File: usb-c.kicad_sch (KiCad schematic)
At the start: 1 part, among them J2 USB-C_GCT_USB4105-GF-A

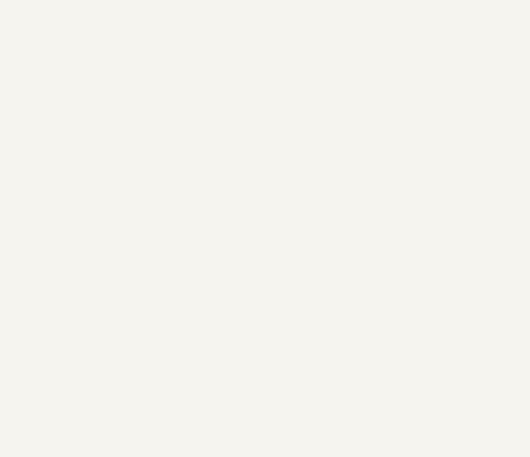
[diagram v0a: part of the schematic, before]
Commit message: [#94684] Add ports to subsheets
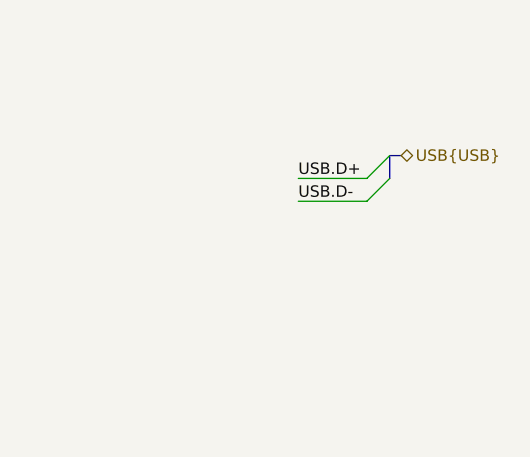
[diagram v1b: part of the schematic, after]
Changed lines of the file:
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@@
 	(generator "eeschema")
 	(generator_version "9.0")
-	(paper "A4")
+	(paper "A3")
 	(title_block
 		(title "renode-reference-platform")
@@
 		(company "Antmicro")
 	)
+	(bus_entry
+		(at 215.9 80.01)
+		(size -2.54 2.54)
+		(stroke
+			(width 0)
+			(type default)
+		)
+	)
+	(bus_entry
+		(at 215.9 77.47)
+		(size -2.54 2.54)
+		(stroke
+			(width 0)
+			(type default)
+		)
+	)
+	(wire
+		(pts
+			(xy 205.74 80.01) (xy 213.36 80.01)
+		)
+		(stroke
+			(width 0)
+			(type default)
+		)
+	)
+	(bus
+		(pts
+			(xy 217.17 77.47) (xy 215.9 77.47)
+		)
+		(stroke
+			(width 0)
+			(type default)
+		)
+	)
+	(wire
+		(pts
+			(xy 205.74 82.55) (xy 213.36 82.55)
+		)
+		(stroke
+			(width 0)
+			(type default)
+		)
+	)
+	(bus
+		(pts
+			(xy 215.9 77.47) (xy 215.9 80.01)
+		)
+		(stroke
+			(width 0)
+			(type default)
+		)
+	)
+	(label "USB.D+"
+		(at 205.74 80.01 0)
+		(effects
+			(font
+				(size 1.27 1.27)
+			)
+			(justify left bottom)
+		)
+	)
+	(label "USB.D-"
+		(at 205.74 82.55 0)
+		(effects
+			(font
+				(size 1.27 1.27)
+			)
+			(justify left bottom)
+		)
+	)
+	(hierarchical_label "USB{USB}"
+		(shape bidirectional)
+		(at 217.17 77.47 0)
+		(effects
+			(font
+				(size 1.27 1.27)
+			)
+			(justify left)
+		)
+	)
 	(symbol

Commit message: [#94911] Add USB DRP
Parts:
- added C42, C44, C45: C_100n_0402, antmicro-footprints:C_0402_1005Metric, symbol antmicroCapacitors0402:C_100n_0402
- added C43: C_4u7_6.3V_0402, antmicro-footprints:C_0402_1005Metric, symbol antmicroCapacitors0402:C_4u7_6.3V_0402
- added D10: PESD5Z5_0F, antmicro-footprints:SOD-523, symbol antmicroTVSDiodes:PESD5Z5_0F
- added D11: TPD2E009_SOT-9X3, antmicro-footprints:SOT-723, symbol antmicroTVSDiodes:TPD2E009_SOT-9X3
- added D8: PRTR5V0U2X, antmicro-footprints:SOT-143-4, symbol antmicroTVSDiodes:PRTR5V0U2X
- added D9: LED_G_0603_LTST-C190GKT, antmicro-footprints:LED_0603_1608Metric_G, symbol antmicroLEDIndicationDiscrete:LED_G_0603_LTST-C190GKT
- added R100, R101, R79, R92, R93, R94, R99: R_0R_0402, antmicro-footprints:R_0402_1005Metric, symbol antmicroResistors0402:R_0R_0402
- added R102, R103: R_100R_0402, antmicro-footprints:R_0402_1005Metric, symbol antmicroResistors0402:R_100R_0402
- added R81: R_330R_0402, antmicro-footprints:R_0402_1005Metric, symbol antmicroResistors0402:R_330R_0402
- added R82: R_12k1_0402, antmicro-footprints:R_0402_1005Metric, symbol antmicroResistors0402:R_12k1_0402
- added R83, R90, R91: R_10k_0402, antmicro-footprints:R_0402_1005Metric, symbol antmicroResistors0402:R_10k_0402
- added R84, R85, R86, R87, R88, R89, R95, R96, R97, R98: R_887k_0402, antmicro-footprints:R_0402_1005Metric, symbol antmicroResistors0402:R_887k_0402
- added TP25, TP26: TP_1mm_SMD, antmicro-footprints:TP_SMD_1mm, symbol antmicroTestPoints:TP_1mm_SMD
- added U12: FUSB303B, antmicro-footprints:Texas_X2QFN-12_1.6x1.6mm_P0.4mm, symbol antmicroInterfaceControllers:FUSB303B
- added U13: AP22615B_TSOT26, antmicro-footprints:TSOT23-6, symbol antmicroPMICPowerDistributionSwitchesLoadDrivers:AP22615B_TSOT26
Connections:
- net USB.D+: now also D8.2 (IO1), R102.2
- net USB.D-: now also D8.3 (IO2), R103.2
- net GND: now reaches J2.A1 (GND), J2.A12 (GND), J2.B1 (GND), J2.B12 (GND)
- net GND: now also J2.SH, C42.1, C43.1, C44.1, C45.1, D10.2 (A), D11.3, D8.1 (GND), D9.1 (C), R82.2, R83.2, R85.1, R87.1, R89.1, R96.1, R98.1, U12.10 (GND), U13.2 (GND)
- net USB_VBUS: now reaches J2.A4 (VBUS), J2.A9 (VBUS), J2.B4 (VBUS), J2.B9 (VBUS)
- net USB_VBUS: now also C42.2, C43.2, D10.1 (C), D8.4 (VCC), R79.2, R81.2, U12.4 (VBUS_{DET}), U13.1 (OUT)
- net CC1: now reaches J2.A5 (CC_{1})
- net CC1: now also D11.1, U12.1 (CC1)
- net at J2.A6 (D_{A}+): now also J2.B6 (D_{B}+), R102.1
- net at J2.A7 (D_{A}-): now also J2.B7 (D_{B}-), R103.1
- net CC2: now reaches J2.B5 (CC_{2})
- net CC2: now also D11.2, U12.2 (CC2)
- new net: R88.1, R89.2, R92.1, R99.1, U12.6 (~{INT}/OUT3)
- new net: R82.1, U13.5 (ISET)
- new net: R100.1, R86.1, R87.2, R93.1, U12.7 (SDA/OUT1)
- new net: R101.1, R84.1, R85.2, R94.1, U12.8 (SCL/OUT2)
- new net: D9.2 (A), R81.1
- new net: R83.1, U12.11 (~{EN})
- new net +3V3: C44.2, R84.2, R86.2, R88.2, R90.1, R91.1, R95.2, R97.2, U12.12 (V_{DD})
- new net +5V: C45.2, U13.6 (IN)
- new net ADDR/ORIENT: R95.1, R96.2, TP25.1, U12.5 (ADDR/ORIENT)
- new net FLG: R90.2, U13.3 (FLG)
- new net I2C_USB.SCL: R94.2
- new net I2C_USB.SDA: R93.2
- new net I2C_USB.~{INT}: R92.2
- new net PORT/~{DEBUG}: R97.1, R98.2, TP26.1, U12.3 (PORT/~{DEBUG})
- new net USB.ID: R91.2, U12.9 (ID), U13.4 (~{EN})
- new net USB.VBUS: R79.1
- new net USB_GPIO_OUT1: R100.2
- new net USB_GPIO_OUT2: R101.2
- new net USB_GPIO_~{INT}: R99.2
- no-connect marks 0 -> 2
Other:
- note added: "R95 - I2C mode address 62h R96 - I2C mode address 42h DNP both for GPIO mode"
- note added: "R97 - Source only R98 - Sink only DNP both for Dual Role Port"
- note added: "limit set to 0.5A"
- moved on the sheet: J2

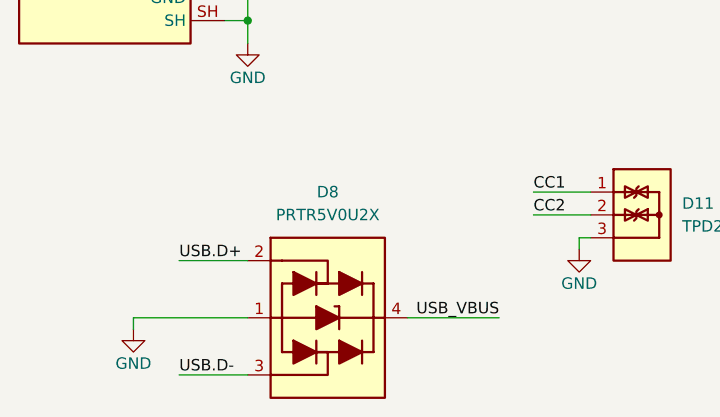
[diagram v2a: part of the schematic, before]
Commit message: [#95008] Change USB-C data lines ESD protection
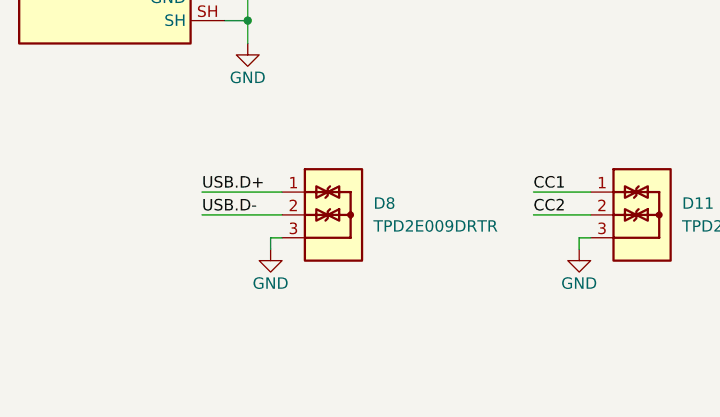
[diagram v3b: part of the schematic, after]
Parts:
- removed D8: PRTR5V0U2X, antmicro-footprints:SOT-143-4, symbol antmicroTVSDiodes:PRTR5V0U2X
- added D8: TPD2E009_SOT-9X3, antmicro-footprints:SOT-723, symbol antmicroTVSDiodes:TPD2E009_SOT-9X3
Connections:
- net GND: now also D8.3
- net USB.D+: now also D8.1
- net USB.D-: now also D8.2

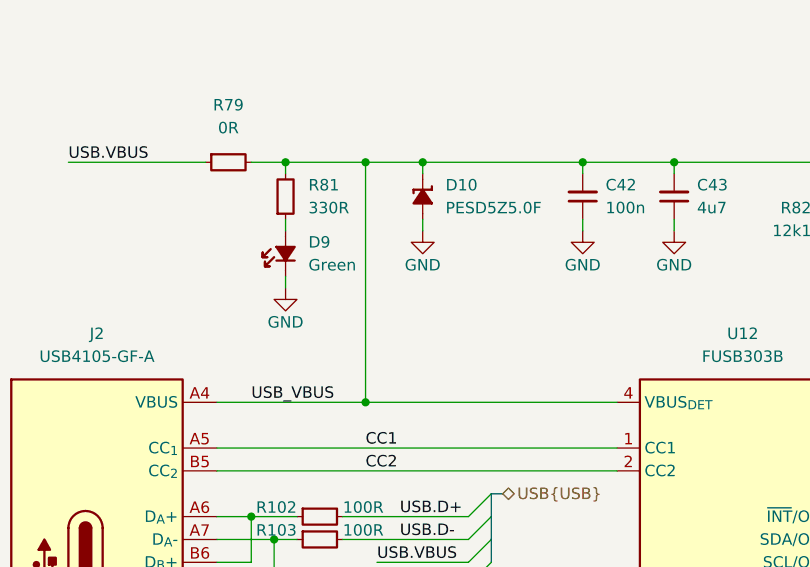
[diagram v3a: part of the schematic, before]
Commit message: [#95036] Reconnect power flags, add GPIOs to RPI connector
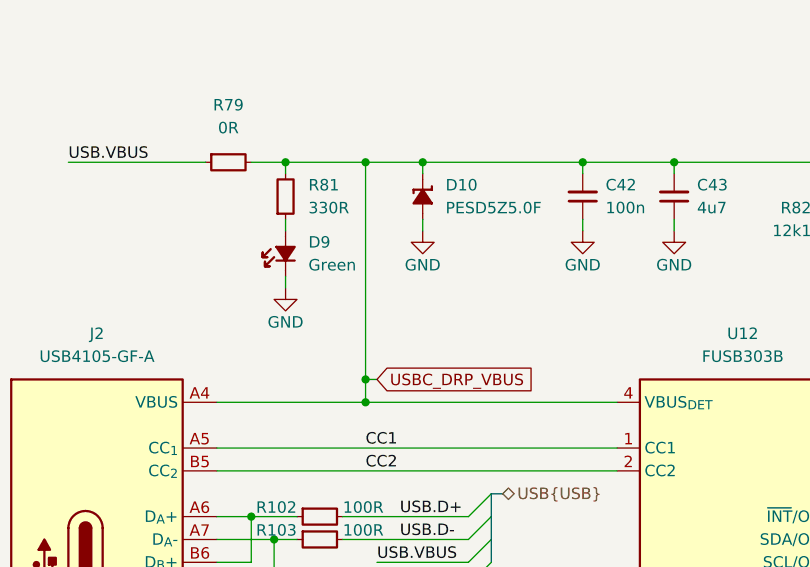
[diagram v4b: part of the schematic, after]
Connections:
- net USB_VBUS renamed USBC_DRP_VBUS
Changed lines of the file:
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@@
+	)
+	(junction
+		(at 144.78 104.14)
+		(diameter 0)
+		(color 0 0 0 0)
 	)
 	(junction
@@
 	(wire
 		(pts
+			(xy 146.05 104.14) (xy 144.78 104.14)
+		)
+		(stroke
+			(width 0)
+			(type default)
+		)
+	)
+	(wire
+		(pts
 			(xy 284.48 168.91) (xy 314.96 168.91)
 		)
@@
 	(wire
 		(pts
-			(xy 144.78 80.01) (xy 144.78 106.68)
+			(xy 144.78 80.01) (xy 144.78 104.14)
 		)
 		(stroke
@@
 		(pts
 			(xy 215.9 82.55) (xy 241.3 82.55)
+		)
+		(stroke
+			(width 0)
+			(type default)
+		)
+	)
+	(wire
+		(pts
+			(xy 144.78 104.14) (xy 144.78 106.68)
 		)
 		(stroke
@@
 		)
 	)
-	(label "USB_VBUS"
-		(at 132.08 106.68 0)
-		(effects
-			(font
-				(size 1.27 1.27)
-			)
-			(justify left bottom)
-		)
-	)
 	(label "USB.ID"
 		(at 222.25 85.09 0)
@@
 		)
 	)
+	(global_label "USBC_DRP_VBUS"
+		(shape input)
+		(at 146.05 104.14 0)
+		(fields_autoplaced yes)
+		(effects
+			(font
+				(size 1.27 1.27)
+				(thickness 0.1588)
+			)
+			(justify left)
+		)
+		(property "Intersheetrefs" "${INTERSHEET_REFS}"
+			(at 164.759 104.14 0)
+			(effects
+				(font
+					(size 1.27 1.27)
+				)
+				(justify left)
+			)
+		)
+	)

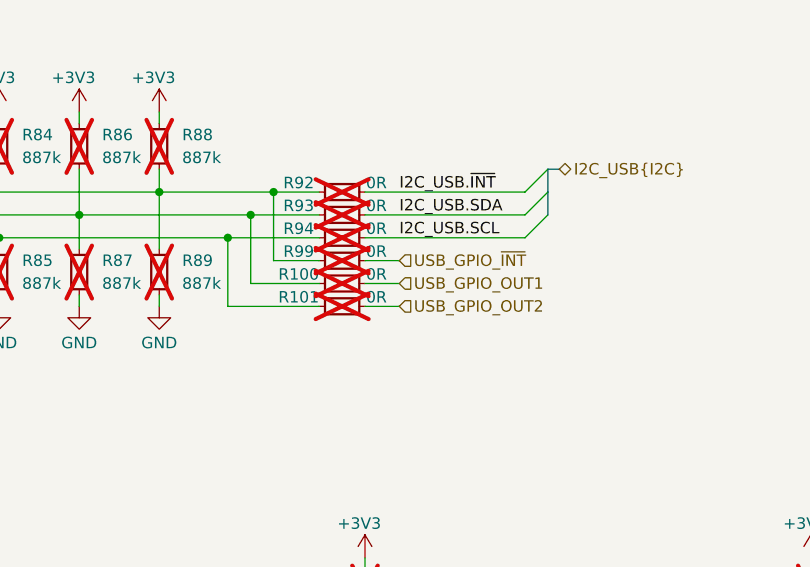
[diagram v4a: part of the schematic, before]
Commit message: [#95036] Manage I2C, UART, SPI interfaces for RPI and PMOD connectors
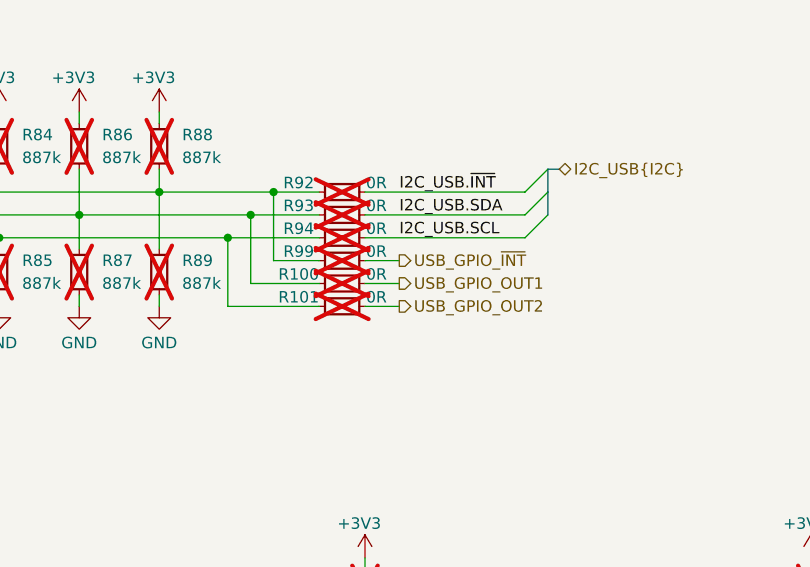
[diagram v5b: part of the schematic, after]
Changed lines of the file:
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@@
 	)
 	(hierarchical_label "USB_GPIO_~{INT}"
-		(shape input)
+		(shape output)
 		(at 269.24 127 0)
 		(effects
@@
 	)
 	(hierarchical_label "USB_GPIO_OUT1"
-		(shape input)
+		(shape output)
 		(at 269.24 129.54 0)
 		(effects
@@
 	)
 	(hierarchical_label "USB_GPIO_OUT2"
-		(shape input)
+		(shape output)
 		(at 269.24 132.08 0)
 		(effects

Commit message: [#95036] Add CAN bus subsheet
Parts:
- removed C43: C_4u7_6.3V_0402, antmicro-footprints:C_0402_1005Metric, symbol antmicroCapacitors0402:C_4u7_6.3V_0402
- added C43: C_4u7_0402, antmicro-footprints:C_0402_1005Metric, symbol antmicroCapacitors0402:C_4u7_0402
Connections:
- net GND: now also C43.1
- net USBC_DRP_VBUS: now also C43.2
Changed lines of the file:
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@@
 	)
 	(symbol
-		(lib_id "antmicroCapacitors0402:C_4u7_6.3V_0402")
-		(at 179.07 86.36 90)
-		(unit 1)
-		(exclude_from_sim no)
-		(in_bom yes)
-		(on_board yes)
-		(dnp no)
-		(fields_autoplaced yes)
-		(property "Reference" "C43"
-			(at 181.61 82.5436 90)
-			(effects
-				(font
-					(size 1.27 1.27)
-					(thickness 0.15)
-				)
-				(justify right)
-			)
-		)
-		(property "Value" "C_4u7_6.3V_0402"
-			(at 189.23 66.04 0)
-			(effects
-				(font
-					(size 1.27 1.27)
-					(thickness 0.15)
-				)
-				(justify left bottom)
-				(hide yes)
-			)
-		)
-		(property "Footprint" "antmicro-footprints:C_0402_1005Metric"
-			(at 191.77 66.04 0)
-			(effects
-				(font
-					(size 1.27 1.27)
-					(thickness 0.15)
-				)
-				(justify left bottom)
-				(hide yes)
-			)
-		)
-		(property "Datasheet" "https://product.samsungsem.com/mlcc/CL05A475KQ5NRN.do"
-			(at 194.31 66.04 0)
-			(effects
-				(font
-					(size 1.27 1.27)
-					(thickness 0.15)
-				)
-				(justify left bottom)
-				(hide yes)
-			)
-		)
-		(property "Description" "SMD Multilayer Ceramic Capacitor, 4.7 µF, 10 V, 0402 [1005 Metric], ± 20%, X5R, GRM Series"
-			(at 212.09 66.04 0)
-			(effects
-				(font
-					(size 1.27 1.27)
-				)
-				(justify left bottom)
-				(hide yes)
-			)
-		)
-		(property "MPN" "CL05A475KQ5NRNC"
-			(at 196.85 66.04 0)
-			(effects
-				(font
-					(size 1.27 1.27)
-					(thickness 0.15)
-				)
-				(justify left bottom)
-				(hide yes)
-			)
-		)
-		(property "Manufacturer" "Samsung Electro-Mechanics"
-			(at 199.39 66.04 0)
-			(effects
-				(font
-					(size 1.27 1.27)
-					(thickness 0.15)
-				)
-				(justify left bottom)
-				(hide yes)
-			)
-		)
-		(property "License" "Apache-2.0"
-			(at 201.93 66.04 0)
-			(effects
-				(font
-					(size 1.27 1.27)
-					(thickness 0.15)
-				)
-				(justify left bottom)
-				(hide yes)
-			)
-		)
-		(property "Author" "Antmicro"
-			(at 204.47 66.04 0)
-			(effects
-				(font
-					(size 1.27 1.27)
-					(thickness 0.15)
-				)
-				(justify left bottom)
-				(hide yes)
-			)
-		)
-		(property "Val" "4u7"
-			(at 181.61 85.0836 90)
-			(effects
-				(font
-					(size 1.27 1.27)
-					(thickness 0.15)
-				)
-				(justify right)
-			)
-		)
-		(property "Voltage" "6.3V"
-			(at 207.01 66.04 0)
-			(effects
-				(font
-					(size 1.27 1.27)
-				)
-				(justify left bottom)
-				(hide yes)
-			)
-		)
-		(property "Dielectric" "X5R"
-			(at 209.55 66.04 0)
-			(effects
-				(font
-					(size 1.27 1.27)
-				)
-				(justify left bottom)
-				(hide yes)
-			)
-		)
-		(pin "2"
-		)
-		(pin "1"
-		)
-		(instances
-			(project "renode-reference-platform"
-				(path "/126ae87b-f292-4372-94ff-ae46971d67ab/ec770658-59a1-4a3f-81ed-5fcccc21c2e8"
-					(reference "C43")
-					(unit 1)
-				)
-			)
-		)
-	)
-	(symbol
 		(lib_id "antmicroResistors0402:R_887k_0402")
 		(at 233.68 130.81 90)
@@
 					(unit 1)
 				)
+			)
+		)
+	)
+	(symbol
+		(lib_id "antmicroCapacitors0402:C_4u7_0402")
+		(at 179.07 86.36 90)
+		(unit 1)
+		(exclude_from_sim no)
+		(in_bom yes)
+		(on_board yes)
+		(dnp no)
+		(fields_autoplaced yes)
+		(property "Reference" "C43"
+			(at 181.61 82.5436 90)
+			(effects
+				(font
+					(size 1.27 1.27)
+					(thickness 0.15)
+				)
+				(justify right)
+			)
+		)
+		(property "Value" "C_4u7_0402"
+			(at 189.23 66.04 0)
+			(effects
+				(font
+					(size 1.27 1.27)
+					(thickness 0.15)
+				)
+				(justify left bottom)
+				(hide yes)
+			)
+		)
+		(property "Footprint" "antmicro-footprints:C_0402_1005Metric"
+			(at 191.77 66.04 0)
+			(effects
+				(font
+					(size 1.27 1.27)
+					(thickness 0.15)
+				)
+				(justify left bottom)
+				(hide yes)
+			)
+		)
+		(property "Datasheet" "https://www.murata.com/products/productdetail?partno=GRM155R61A475MEAA%23"
+			(at 194.31 66.04 0)
+			(effects
+				(font
+					(size 1.27 1.27)
+					(thickness 0.15)
+				)
+				(justify left bottom)
+				(hide yes)
+			)
+		)
+		(property "Description" "SMD Multilayer Ceramic Capacitor, 4.7 µF, 10 V, 0402 [1005 Metric], ± 20%, X5R, GRM Series"
+			(at 212.09 66.04 0)
+			(effects
+				(font
+					(size 1.27 1.27)
+				)
+				(justify left bottom)
+				(hide yes)
+			)
+		)
+		(property "MPN" "GRM155R61A475MEAAD"
+			(at 196.85 66.04 0)
+			(effects
+				(font
+					(size 1.27 1.27)
+					(thickness 0.15)
+				)
+				(justify left bottom)
+				(hide yes)
+			)
+		)
+		(property "Manufacturer" "Murata"
+			(at 199.39 66.04 0)
+			(effects
+				(font
+					(size 1.27 1.27)
+					(thickness 0.15)
+				)
+				(justify left bottom)
+				(hide yes)
+			)
+		)
+		(property "License" "Apache-2.0"
+			(at 201.93 66.04 0)
+			(effects
+				(font
+					(size 1.27 1.27)
+					(thickness 0.15)
+				)
+				(justify left bottom)
+				(hide yes)
+			)
+		)
+		(property "Author" "Antmicro"
+			(at 204.47 66.04 0)
+			(effects
+				(font
+					(size 1.27 1.27)
+					(thickness 0.15)
+				)
+				(justify left bottom)
+				(hide yes)
+			)
+		)
+		(property "Val" "4u7"
+			(at 181.61 85.0836 90)
+			(effects
+				(font
+					(size 1.27 1.27)
+					(thickness 0.15)
+				)
+				(justify right)
+			)
+		)
+		(property "Voltage" ""
+			(at 207.01 66.04 0)
+			(effects
+				(font
+					(size 1.27 1.27)
+				)
+				(justify left bottom)
+				(hide yes)
+			)
+		)
+		(property "Dielectric" ""
+			(at 209.55 66.04 0)
+			(effects
+				(font
+					(size 1.27 1.27)
+				)
+				(justify left bottom)
+				(hide yes)
+			)
+		)
+		(pin "1"
+		)
+		(pin "2"
+		)
+		(instances
+			(project "renode-reference-platform"
+				(path "/126ae87b-f292-4372-94ff-ae46971d67ab/ec770658-59a1-4a3f-81ed-5fcccc21c2e8"
+					(reference "C43")
+					(unit 1)
+				)
